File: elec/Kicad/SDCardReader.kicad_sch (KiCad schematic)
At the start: 0 parts

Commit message: merci Linux
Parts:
- added C5: 100nF, symbol Device:C_Polarized
- added J1: SD_Card_Device, symbol Connector:SD_Card_Device
- added R4, R5, R6, R7: 10K, symbol Device:R
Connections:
- new net: J1.8 (DAT1), R6.2
- new net: J1.9 (DAT2), R5.2
- new net +3.3V: C5.1, J1.4 (VDD), R4.1, R5.1, R6.1, R7.1
- new net CS: J1.1 (CD/DAT3), R4.2
- new net GND: C5.2, J1.3 (VSS), J1.6 (VSS)
- new net MISO: J1.7 (DAT0), R7.2
- new net MOSI: J1.2 (CMD)
- new net SCK: J1.5 (CLK)
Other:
- note added: "Jpense que au final on s'en fou si c'est pas un polariser"
- note added: "en théorie 10 GPIO"

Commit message: sa progresse. Battery management fini + humidity/temp sensor + bouton
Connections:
- net CS renamed CS_SD
- net MISO renamed SPI1_MISO
- net MOSI renamed SPI1_MOSI
- net SCK renamed SPI1_SCK
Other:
- moved on the sheet: C5, R4, R5, R6

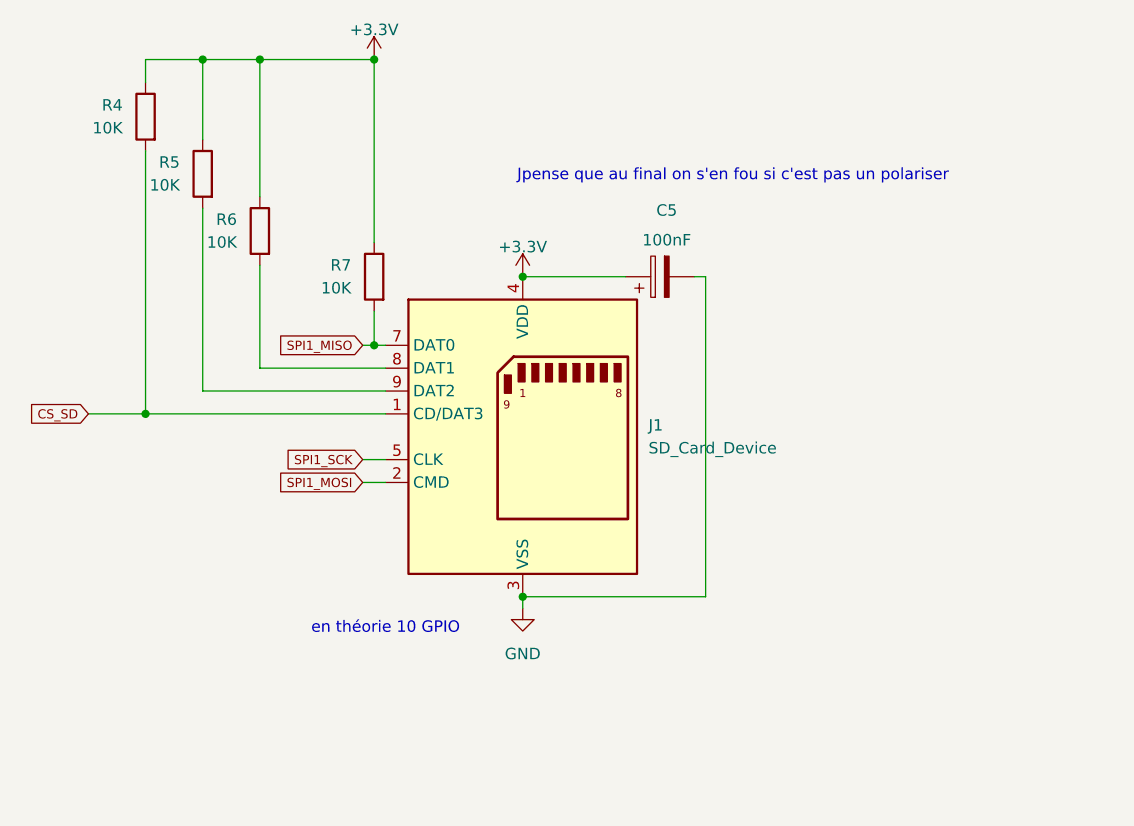
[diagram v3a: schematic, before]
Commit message: add a few footprint
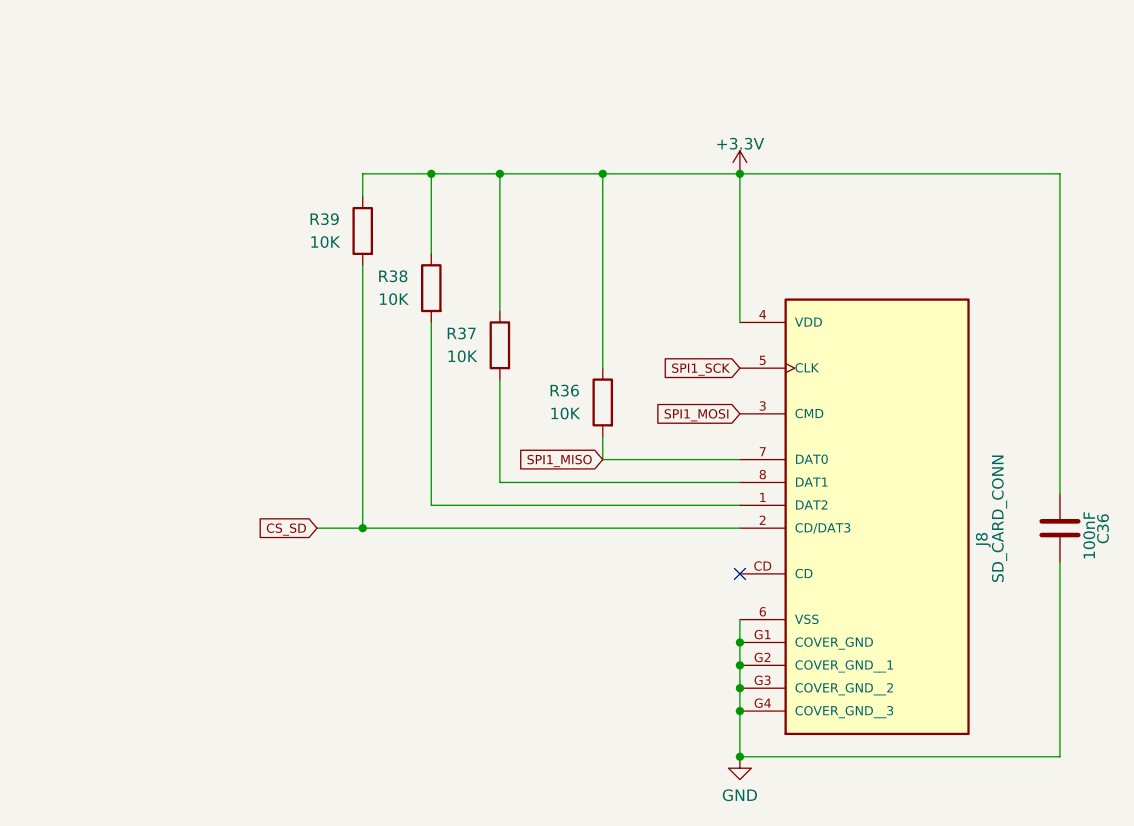
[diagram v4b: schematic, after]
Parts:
- removed C5: 100nF, symbol Device:C_Polarized
- removed J1: SD_Card_Device, symbol Connector:SD_Card_Device
- removed R4, R5, R6, R7: 10K, symbol Device:R
- added C36: 100nF, Capacitor_SMD:C_0603_1608Metric_Pad1.08x0.95mm_HandSolder, symbol Device:C
- added J8: SD_CARD_CONN, MSD_4_A_SD:CUI_MSD-4-A, symbol MSD-4-A:MSD-4-A
- added R36, R37, R38, R39: 10K, Resistor_SMD:R_0603_1608Metric_Pad0.98x0.95mm_HandSolder, symbol Device:R
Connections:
- net +3.3V: now also C36.1, J8.4 (VDD), R36.1, R37.1, R38.1, R39.1
- net CS_SD: now also J8.2 (CD/DAT3), R39.2
- net GND: now also C36.2, J8.6 (VSS), J8.G1 (COVER_GND), J8.G2 (COVER_GND__1), J8.G3 (COVER_GND__2), J8.G4 (COVER_GND__3)
- net SPI1_MISO: now also J8.7 (DAT0), R36.2
- net SPI1_MOSI: now also J8.3 (CMD)
- net SPI1_SCK: now also J8.5 (CLK)
- new net: J8.1 (DAT2), R38.2
- new net: J8.8 (DAT1), R37.2
- no-connect marks 0 -> 1
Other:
- note removed: "Jpense que au final on s'en fou si c'est pas un polariser"
- note removed: "en théorie 10 GPIO"

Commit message: Jpense pas boire jeudi sérieux vue que y'a pas de 5@8
routage du découplage et des CLK
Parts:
- C36: footprint Capacitor_SMD:C_0603_1608Metric_Pad1.08x0.95mm_HandSolder -> Capacitor_SMD:C_0402_1005Metric_Pad0.74x0.62mm_HandSolder
- R36, R37, R38, R39: footprint Resistor_SMD:R_0603_1608Metric_Pad0.98x0.95mm_HandSolder -> Resistor_SMD:R_0402_1005Metric_Pad0.72x0.64mm_HandSolder
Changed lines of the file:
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@@
 			)
 		)
-		(property "Footprint" "Resistor_SMD:R_0603_1608Metric_Pad0.98x0.95mm_HandSolder"
+		(property "Footprint" "Resistor_SMD:R_0402_1005Metric_Pad0.72x0.64mm_HandSolder"
 			(at 69.088 57.15 90)
 			(effects
@@
 			)
 		)
-		(property "Footprint" "Resistor_SMD:R_0603_1608Metric_Pad0.98x0.95mm_HandSolder"
+		(property "Footprint" "Resistor_SMD:R_0402_1005Metric_Pad0.72x0.64mm_HandSolder"
 			(at 61.468 50.8 90)
 			(effects
@@
 			)
 		)
-		(property "Footprint" "Resistor_SMD:R_0603_1608Metric_Pad0.98x0.95mm_HandSolder"
+		(property "Footprint" "Resistor_SMD:R_0402_1005Metric_Pad0.72x0.64mm_HandSolder"
 			(at 53.848 44.45 90)
 			(effects
@@
 			)
 		)
-		(property "Footprint" "Capacitor_SMD:C_0603_1608Metric_Pad1.08x0.95mm_HandSolder"
+		(property "Footprint" "Capacitor_SMD:C_0402_1005Metric_Pad0.74x0.62mm_HandSolder"
 			(at 130.5052 81.28 0)
 			(effects
@@
 			)
 		)
-		(property "Footprint" "Resistor_SMD:R_0603_1608Metric_Pad0.98x0.95mm_HandSolder"
+		(property "Footprint" "Resistor_SMD:R_0402_1005Metric_Pad0.72x0.64mm_HandSolder"
 			(at 80.518 63.5 90)
 			(effects

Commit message: généré la schematic
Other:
- note added: "SPI micro SD socket"
- company: (none) -> University of Sherbrooke
- title: (none) -> Touillometre - SD Card Reader
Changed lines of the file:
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@@
 	(generator_version "8.0")
 	(paper "A4")
+	(title_block
+		(title "Touillometre - SD Card Reader")
+		(date "2024-12-26")
+		(rev "C3I")
+		(company "University of Sherbrooke")
+	)
 	(junction
 		(at 93.98 97.79)
@@
 		)
 	)
+	(text "SPI micro SD socket"
+		(exclude_from_sim no)
+		(at 91.44 26.924 0)
+		(effects
+			(font
+				(size 1.27 1.27)
+			)
+		)
+	)
